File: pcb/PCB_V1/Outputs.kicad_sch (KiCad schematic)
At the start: 21 parts, among them J501 FAN1 / 3.5 mm, J511 FAN2 / 3.5 mm, J521 PUMP 24V / 6W, Q501 AO3400A, Q511 AO3400A, Q521 AO3422

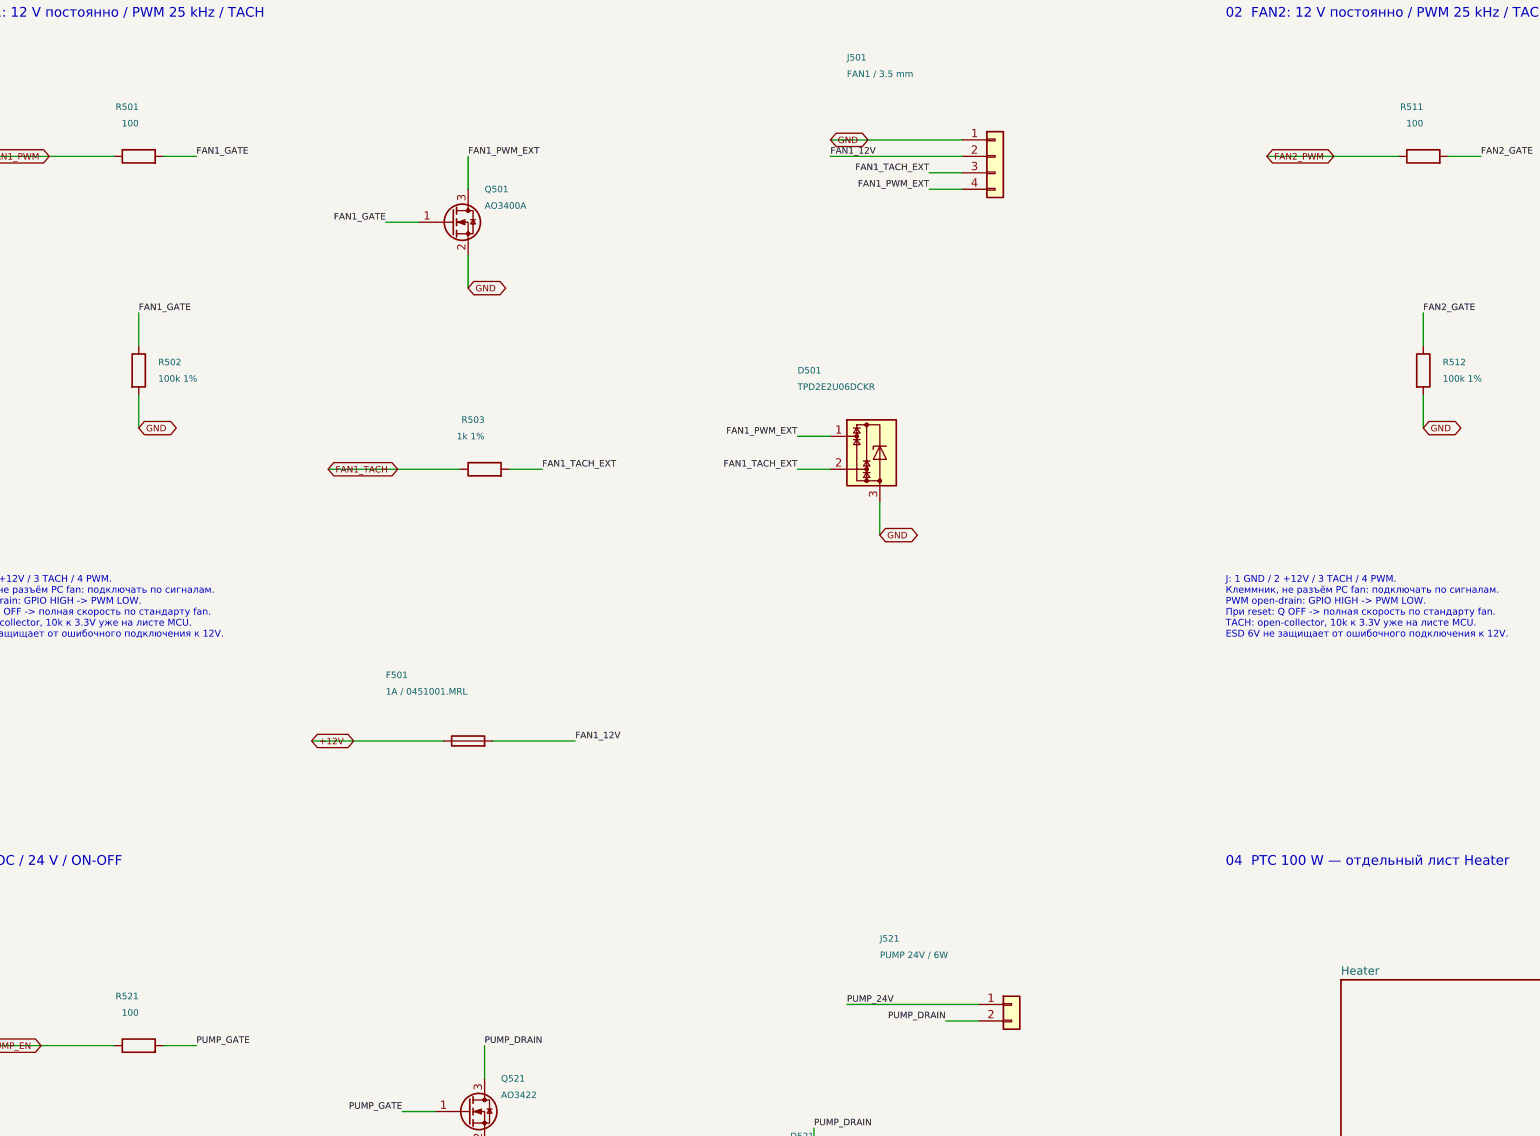
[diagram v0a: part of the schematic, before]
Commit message: pcb: revision 0.19 cost-down in the schematic, same footprints
Schematic and calculations only; PCB_V1.kicad_pcb is untouched on the
user's request. All substitutions keep footprints and nets.

- C716-C719, C726-C728: TDK C3225X7R2A106K250AC (X7R, published DC-bias
  curve 2.35 uF at 49 V) instead of Samsung CL32Y106KCV6PNE.
- C104/C105/C401: Samsung CL21A226MPQNNNE X5R; C521/C710/C715/C725/
  C905/C906: Taiyo Yuden UMK325AB7106KMHP.
- C602 shares CL21A106KAYNNNE with C201 (1.41 uF screen >= 1 uF);
  D601 shares SMBJ26CA with D901 (D_TVS symbol, 42.1 V clamp);
  R501/R511/R521 33R; F904 3 A shared with F721.
- analyze_led_power/analyze_power_path/verify_netlist updated; price and
  JLC snapshots v19; reports, sheet images and checks log v19.
- COST_DOWN.md: USD 37.50 per board (was 39.82), 65 purchase codes,
  rejected candidates and board status.

verify_board.py reports value differences for 17 parts until the board
is synced (footprints and nets already match); all other checks pass.

Co-Authored-By: Claude Opus 5.5 <noreply@anthropic.com>
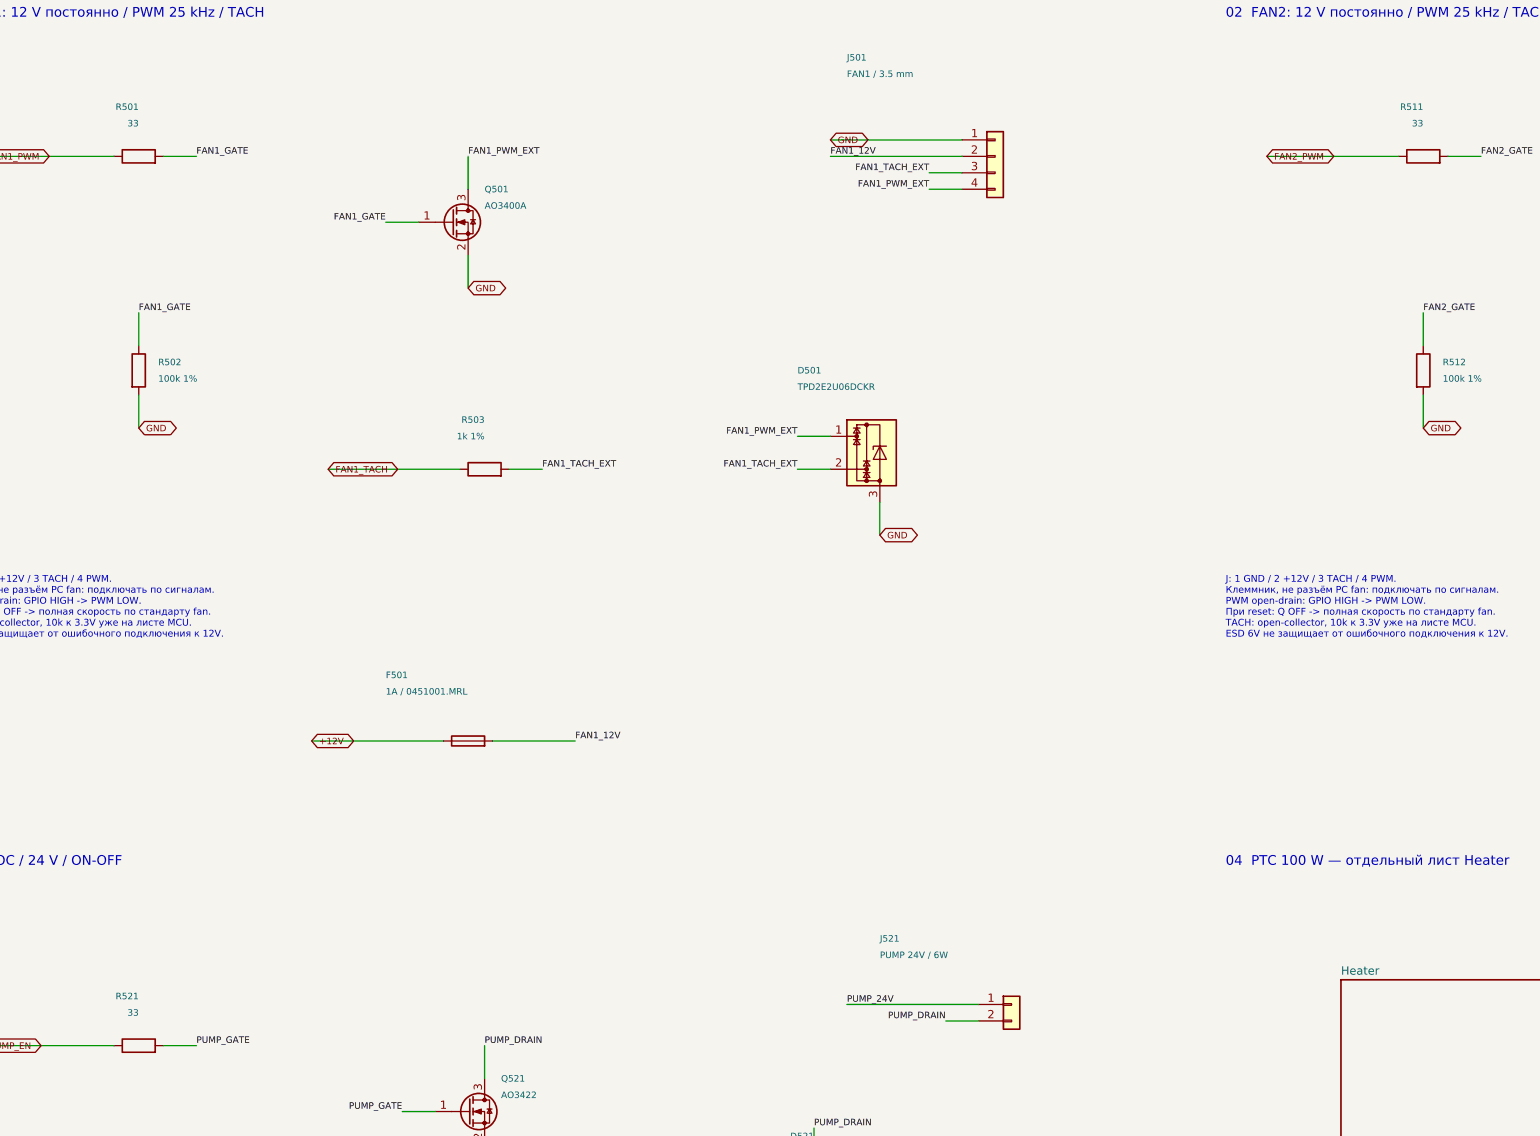
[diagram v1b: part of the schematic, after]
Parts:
- C521: LCSC C77102 -> C386166; MPN GRM32ER71H106KA12L -> UMK325AB7106KMHP; Manufacturer Murata -> Taiyo Yuden
- R501, R511, R521: value 100 -> 33
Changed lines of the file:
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@@
 			)
 		)
-		(property "Value" "100"
+		(property "Value" "33"
 			(at 248.92 55.88 90)
 			(show_name no)
@@
 			)
 		)
-		(property "Value" "100"
+		(property "Value" "33"
 			(at 50.8 55.88 90)
 			(show_name no)
@@
 			)
 		)
-		(property "Datasheet" ""
+		(property "Datasheet" "https://ds.yuden.co.jp/TYCOMPAS/ut/detail?pn=UMK325AB7106KMHP"
 			(at 101.6 243.84 0)
 			(hide yes)
@@
 			)
 		)
-		(property "LCSC" "C77102"
+		(property "LCSC" "C386166"
 			(at 101.6 243.84 0)
 			(effects
@@
 			)
 		)
-		(property "MPN" "GRM32ER71H106KA12L"
+		(property "MPN" "UMK325AB7106KMHP"
 			(at 101.6 243.84 0)
 			(effects
@@
 			)
 		)
-		(property "Manufacturer" "Murata"
+		(property "Manufacturer" "Taiyo Yuden"
 			(at 101.6 243.84 0)
 			(effects
@@
 			)
 		)
-		(property "Value" "100"
+		(property "Value" "33"
 			(at 50.8 193.04 90)
 			(show_name no)

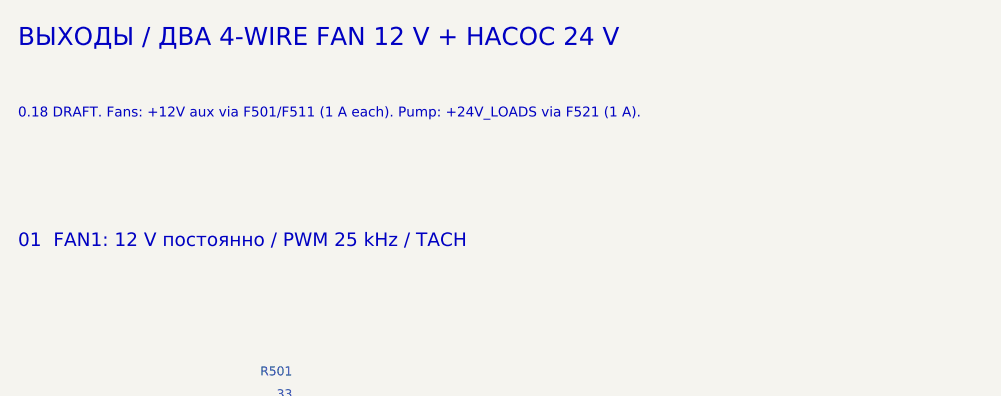
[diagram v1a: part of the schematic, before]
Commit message: pcb: revision 0.20 cost-down with new footprints and placement
- RTC: DS3231MZ replaced by NXP PCF8563T/5 with an Epson FC-135 crystal
  (CL 12.5 pF), C304 18 pF C0G on OSCI, BAT54C supply OR (D303) and R307
  1k from the CR2032.
- Boost switches Q711/Q721: AOS AOD66923 (DPAK) on a project footprint
  that keeps the S1/2/3 G4 D5 numbering; diodes D711/D721: Vishay SS5P10
  (TO-277A).
- L101 cjiang FXL0630-100-M and L902 PROD PSPMAA0604-220M-ANP on the
  KiCad FXL0630 land.
- LED switch areas and the RTC cluster re-placed (29 parts moved);
  ERC 0, DRC 0, 340 unrouted links.
- Checks, price/JLC snapshots v20, reports, placement images and docs
  updated: USD 31.62 per board (29.52 for five boards).

Co-Authored-By: Claude Opus 5.5 <noreply@anthropic.com>
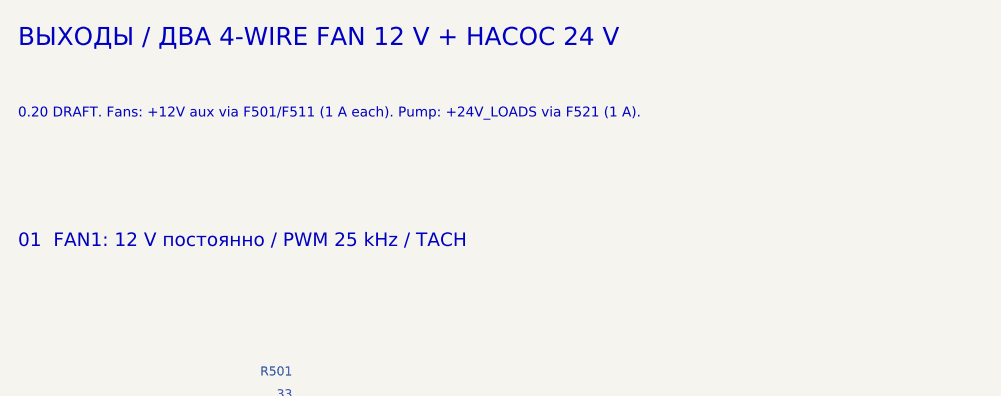
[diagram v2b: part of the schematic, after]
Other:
- note added: "0.20 DRAFT. Fans: +12V aux via F501/F511 (1 A each). Pump: +24V_LOADS via F521 (1 A)."
- note removed: "0.18 DRAFT. Fans: +12V aux via F501/F511 (1 A each). Pump: +24V_LOADS via F521 (1 A)."
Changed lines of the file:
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@@
 		(title "04 - Fans (12 V aux) and pump (24 V)")
 		(date "2026-09-29")
-		(rev "0.18-DRAFT")
+		(rev "0.20-DRAFT")
 		(company "GrowBox controller")
 		(comment 1 "Simplified prototype; unrouted; hardware qualification pending")
@@
 		)
 	)
-	(text "0.18 DRAFT. Fans: +12V aux via F501/F511 (1 A each). Pump: +24V_LOADS via F521 (1 A)."
+	(text "0.20 DRAFT. Fans: +12V aux via F501/F511 (1 A each). Pump: +24V_LOADS via F521 (1 A)."
 		(exclude_from_sim no)
 		(at 20.32 24.13 0)
